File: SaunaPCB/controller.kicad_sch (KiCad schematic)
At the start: 17 parts, among them J301 KL2RM5.08, J302 KL2RM5.08, J303 KL2RM5.08, J304 KL2RM5.08, J305 B4B-ZR, J306 B5B-ZR, U301 ESP32-DEVKITC, U302 ULN2003

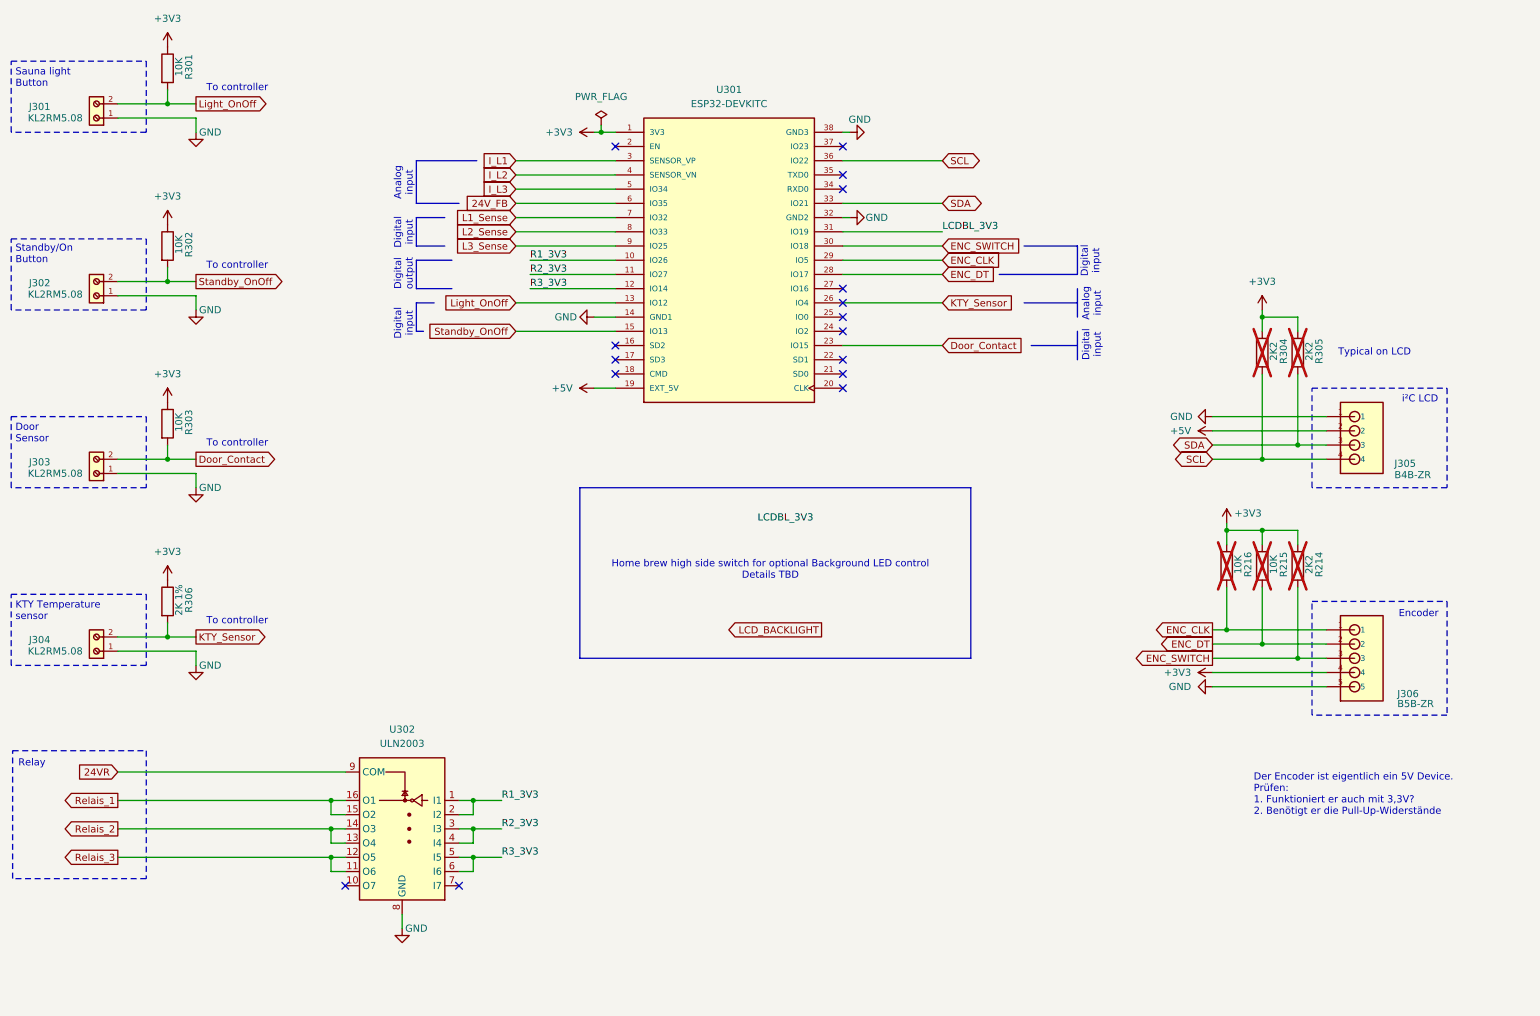
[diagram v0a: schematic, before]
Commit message: ^MOV and Fuse added
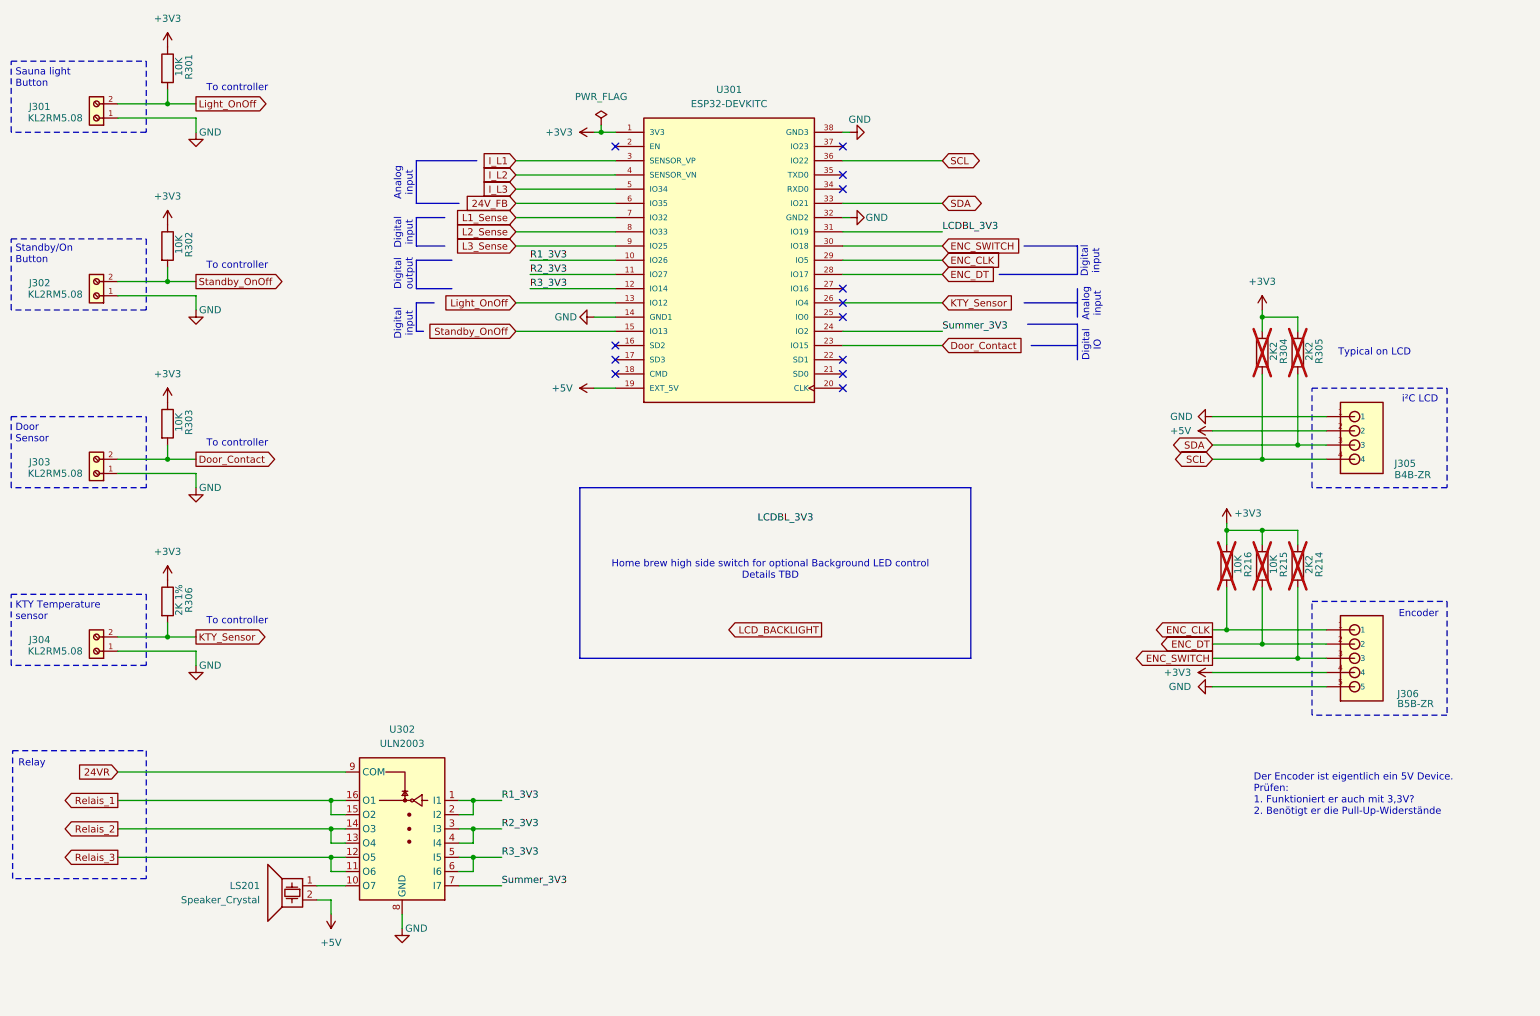
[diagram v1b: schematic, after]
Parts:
- added LS201: Speaker_Crystal, Buzzer_Beeper:Buzzer_TDK_PS1240P02BT_D12.2mm_H6.5mm, symbol Device:Speaker_Crystal
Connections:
- net +5V: now also LS201.2
- net at U302.10 (O7): now also LS201.1
- net Summer_3V3: now reaches U302.7 (I7)
- net Summer_3V3: now also U301.24 (IO2)
- no-connect marks 16 -> 13
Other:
- note added: "Digital IO"
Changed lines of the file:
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@@
 		)
 	)
-	(text "Digital\ninput"
+	(text "Digital\nIO"
 		(exclude_from_sim no)
 		(at 212.09 76.2 90)
@@
 	)
 	(no_connect
-		(at 167.64 73.66)
-	)
-	(no_connect
 		(at 167.64 71.12)
 	)
 	(no_connect
-		(at 99.06 172.72)
-	)
-	(no_connect
 		(at 167.64 81.28)
 	)
@@
 		(at 167.64 66.04)
 	)
-	(no_connect
-		(at 78.74 172.72)
-	)
 	(wire
 		(pts
@@
 	(wire
 		(pts
+			(xy 73.66 172.72) (xy 78.74 172.72)
+		)
+		(stroke
+			(width 0)
+			(type default)
+		)
+	)
+	(wire
+		(pts
 			(xy 52.07 35.56) (xy 52.07 38.1)
 		)
@@
 	(wire
 		(pts
+			(xy 73.66 175.26) (xy 76.2 175.26)
+		)
+		(stroke
+			(width 0)
+			(type default)
+		)
+	)
+	(wire
+		(pts
 			(xy 111.76 60.96) (xy 127 60.96)
 		)
@@
 	(wire
 		(pts
+			(xy 76.2 175.26) (xy 76.2 177.8)
+		)
+		(stroke
+			(width 0)
+			(type default)
+		)
+	)
+	(wire
+		(pts
 			(xy 109.22 73.66) (xy 127 73.66)
 		)
@@
 	(wire
 		(pts
+			(xy 99.06 172.72) (xy 106.68 172.72)
+		)
+		(stroke
+			(width 0)
+			(type default)
+		)
+	)
+	(wire
+		(pts
 			(xy 233.68 88.9) (xy 254 88.9)
 		)
@@
 	(wire
 		(pts
+			(xy 167.64 73.66) (xy 185.42 73.66)
+		)
+		(stroke
+			(width 0)
+			(type default)
+		)
+	)
+	(wire
+		(pts
 			(xy 236.22 109.22) (xy 242.57 109.22)
 		)
@@
 		)
 	)
+	(polyline
+		(pts
+			(xy 200.66 72.39) (xy 209.55 72.39)
+		)
+		(stroke
+			(width 0)
+			(type default)
+		)
+	)
 	(wire
 		(pts
@@
 	(polyline
 		(pts
-			(xy 209.55 73.66) (xy 209.55 78.74)
+			(xy 209.55 72.39) (xy 209.55 78.74)
 		)
 		(stroke
@@
 		)
 	)
+	(label "Summer_3V3"
+		(at 185.42 73.66 0)
+		(effects
+			(font
+				(size 1.27 1.27)
+			)
+			(justify left bottom)
+		)
+	)
+	(label "Summer_3V3"
+		(at 106.68 172.72 0)
+		(effects
+			(font
+				(size 1.27 1.27)
+			)
+			(justify left bottom)
+		)
+	)
 	(label "R3_3V3"
 		(at 111.76 66.04 0)
@@
 	)
 	(symbol
+		(lib_id "Device:Speaker_Crystal")
+		(at 68.58 172.72 0)
+		(mirror y)
+		(unit 1)
+		(exclude_from_sim no)
+		(in_bom yes)
+		(on_board yes)
+		(dnp no)
+		(property "Reference" "LS201"
+			(at 63.5 172.7199 0)
+			(effects
+				(font
+					(size 1.27 1.27)
+				)
+				(justify left)
+			)
+		)
+		(property "Value" "Speaker_Crystal"
+			(at 63.5 175.2599 0)
+			(effects
+				(font
+					(size 1.27 1.27)
+				)
+				(justify left)
+			)
+		)
+		(property "Footprint" "Buzzer_Beeper:Buzzer_TDK_PS1240P02BT_D12.2mm_H6.5mm"
+			(at 69.469 173.99 0)
+			(effects
+				(font
+					(size 1.27 1.27)
+				)
+				(hide yes)
+			)
+		)
+		(property "Datasheet" "~"
+			(at 69.469 173.99 0)
+			(effects
+				(font
+					(size 1.27 1.27)
+				)
+				(hide yes)
+			)
+		)
+		(property "Description" "Crystal speaker/transducer"
+			(at 68.58 172.72 0)
+			(effects
+				(font
+					(size 1.27 1.27)
+				)
+				(hide yes)
+			)
+		)
+		(pin "2"
+		)
+		(pin "1"
+		)
+		(instances
+			(project ""
+				(path "/e6d8484d-2bb5-441d-9b2b-e37a9f2fa458/8da01db6-a1a1-4b01-9382-9f6e5fdc0347"
+					(reference "LS201")
+					(unit 1)
+				)
+			)
+		)
+	)
+	(symbol
 		(lib_id "Device:R")
 		(at 242.57 77.47 0)
@@
 					(unit 1)
 				)
+			)
+		)
+	)
+	(symbol
+		(lib_id "power:+5V")
+		(at 76.2 177.8 180)
+		(unit 1)
+		(exclude_from_sim no)
+		(in_bom yes)
+		(on_board yes)
+		(dnp no)
+		(fields_autoplaced yes)
+		(property "Reference" "#PWR0220"
+			(at 76.2 173.99 0)
+			(effects
+				(font
+					(size 1.27 1.27)
+				)
+				(hide yes)
+			)
+		)
+		(property "Value" "+5V"
+			(at 76.2 182.88 0)
+			(effects
+				(font
+					(size 1.27 1.27)
+				)
+			)
+		)
+		(property "Footprint" ""
+			(at 76.2 177.8 0)
+			(effects
+				(font
+					(size 1.27 1.27)
+				)
+				(hide yes)
+			)
+		)
+		(property "Datasheet" ""
+			(at 76.2 177.8 0)
+			(effects
+				(font
+					(size 1.27 1.27)
+				)
+				(hide yes)
+			)
+		)
+		(property "Description" "Power symbol creates a global label with name \"+5V\""
+			(at 76.2 177.8 0)
+			(effects
+				(font
+					(size 1.27 1.27)
+				)
+				(hide yes)
+			)
+		)
+		(pin "1"
+		)
+		(instances
+			(project "SaunaPCB"
+				(path "/e6d8484d-2bb5-441d-9b2b-e37a9f2fa458/8da01db6-a1a1-4b01-9382-9f6e5fdc0347"
+					(reference "#PWR0220")
+					(unit 1)
+				)

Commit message: Power LED changed to JST connector KTY room added
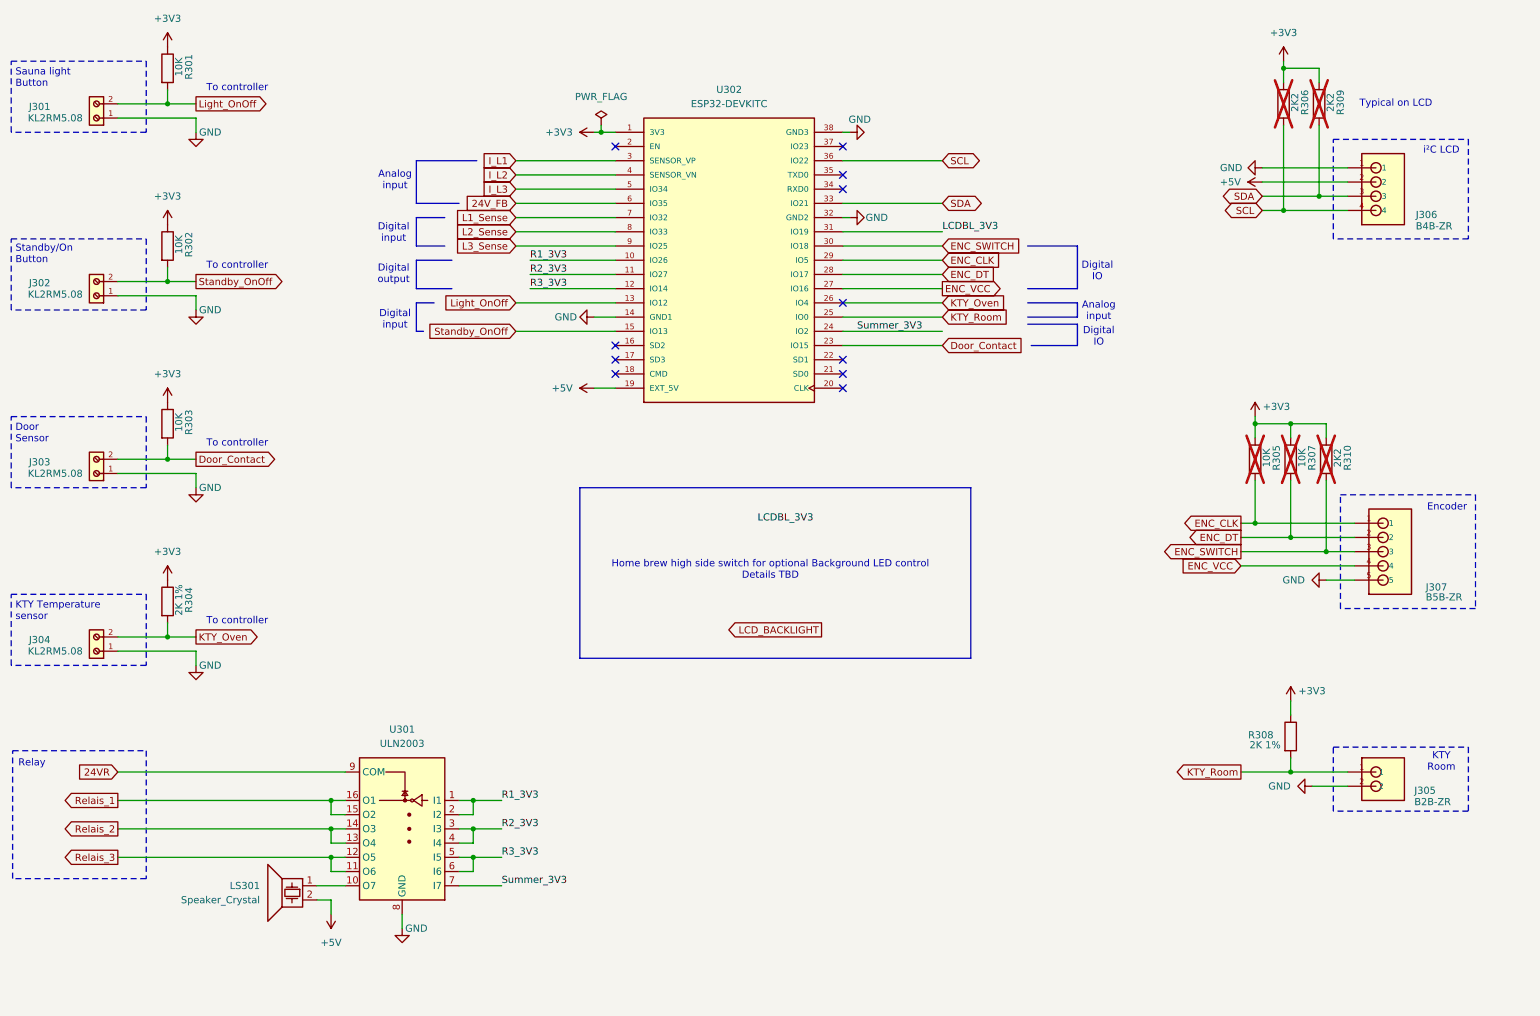
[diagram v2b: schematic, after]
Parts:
- added J305: B2B-ZR, MyConnectors:B2B-ZR, symbol MyConnectors:B2B-ZR
- added R308: 2K 1%, Resistor_SMD:R_1206_3216Metric, symbol Device:R
- renumbered J305 to J306, J306 to J307, LS201 to LS301, R306 to R304, R216 to R305, R304 to R306, R215 to R307, R305 to R309, R214 to R310, U302 to U301, U301 to U302
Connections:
- net +3V3: now also R308.1; no longer J307.4
- net GND: now also J305.2
- net KTY_Room: now reaches U302.25 (IO0)
- net KTY_Room: now also J305.1, R308.2
- net ENC_VCC: now reaches U302.27 (IO16)
- net ENC_VCC: now also J307.4
- net KTY_Sensor renamed KTY_Oven
- no-connect marks 13 -> 11
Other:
- note added: "KTY Room"
- note removed: "Der Encoder ist eigentlich ein 5V Device. Prüfen: 1. Funktioniert er auch mit 3,3V? 2. Benötigt er die Pull-Up-Widerstände"
- moved on the sheet: J306, J307, R305, R306, R307, R309, R310

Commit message: Backlight signal removed two debug pins added remarks regarding KTY added
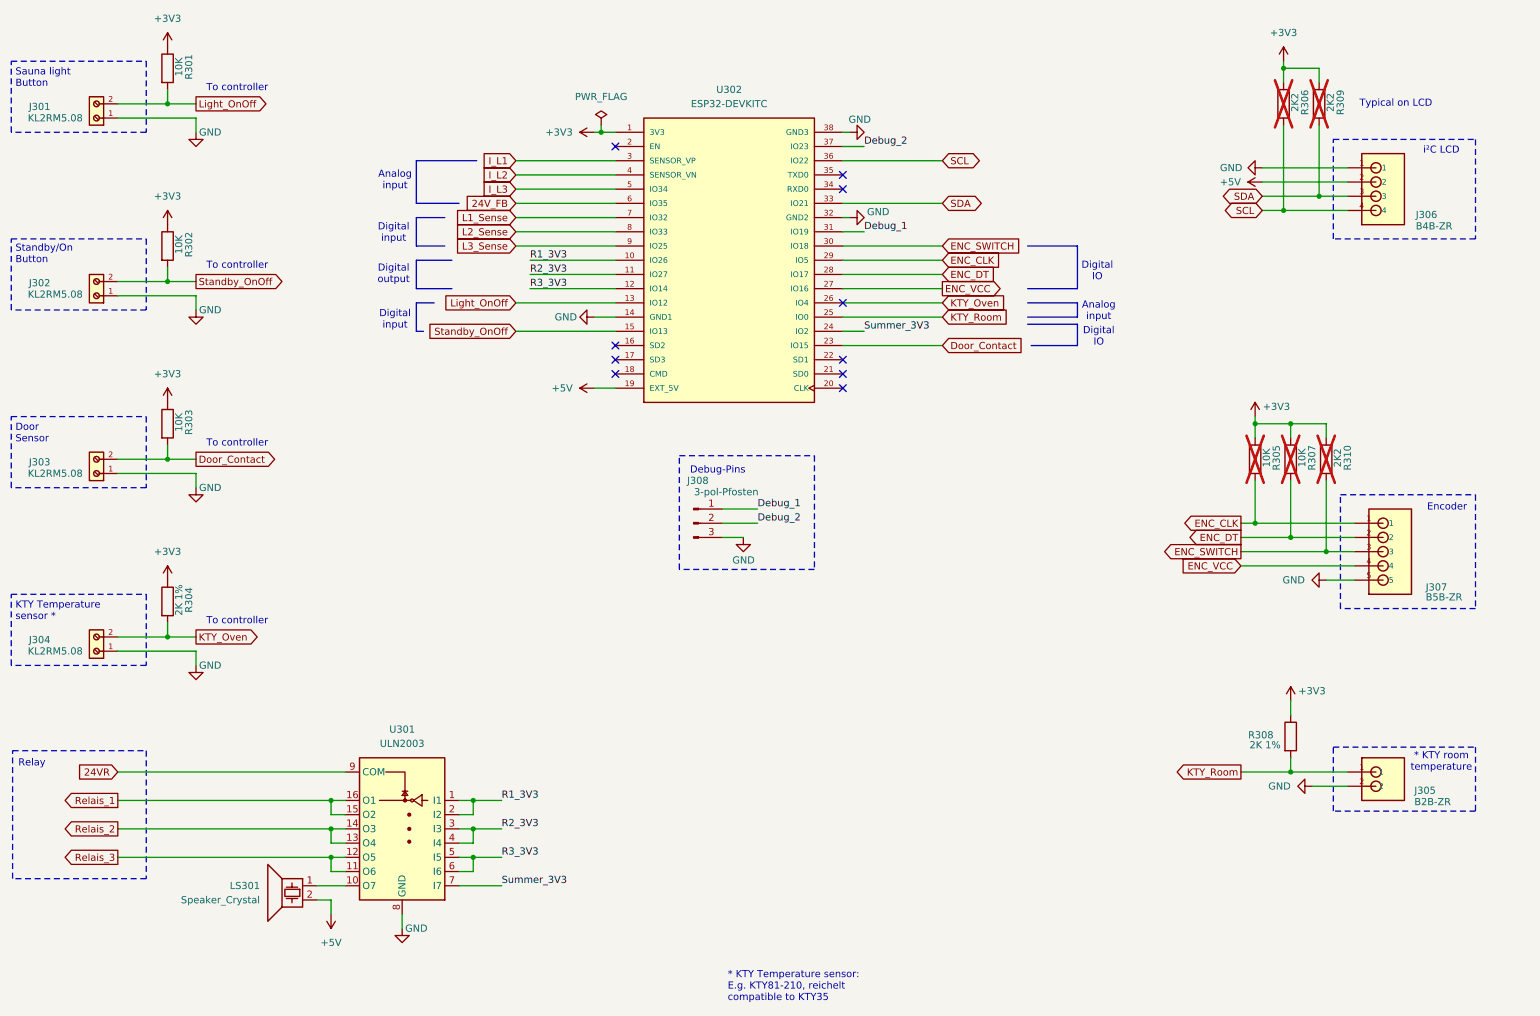
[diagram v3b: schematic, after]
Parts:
- added J308: 3-pol-Pfosten, Connector_PinHeader_1.00mm:PinHeader_1x03_P1.00mm_Vertical, symbol Connector:Conn_01x03_Pin
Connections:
- net GND: now also J308.3 (Pin_3)
- net Debug_2: now reaches U302.37 (IO23)
- net Debug_2: now also J308.2 (Pin_2)
- net LCDBL_3V3 renamed Debug_1
- net Debug_1: now also J308.1 (Pin_1)
- no-connect marks 11 -> 10
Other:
- note added: "* KTY Temperature sensor: E.g. KTY81-210, reichelt compatible to KTY35"
- note added: "* KTY room temperature"
- note added: "Debug-Pins"
- note added: "KTY Temperature sensor *"
- note removed: "Home brew high side switch for optional Background LED control Details TBD"
- note removed: "KTY Room"
- note removed: "KTY Temperature sensor"
